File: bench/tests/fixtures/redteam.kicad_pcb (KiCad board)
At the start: 2 copper layers, 40 x 20 mm, 3 parts

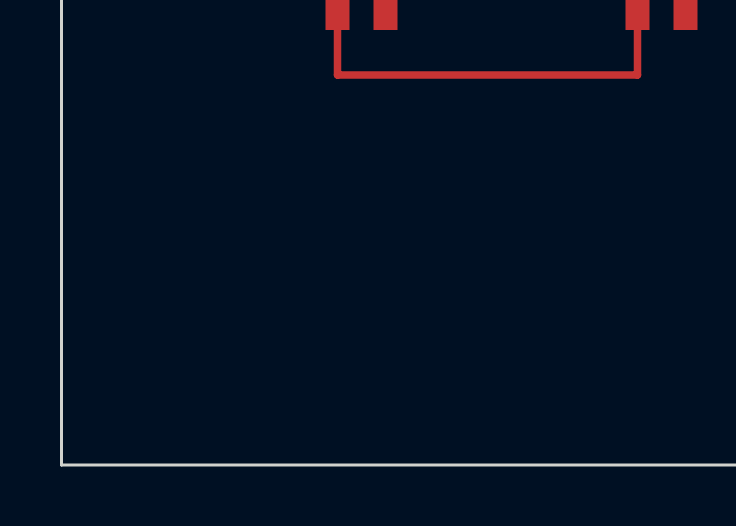
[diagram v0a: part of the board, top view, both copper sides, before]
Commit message: prepare: strip teardrops with the routing; unique footprint uuids (task spec 3)
Found by running the human reference over the 2,491 qualified boards of the
local corpus:

- Teardrops are zones KiCad generates at track ends. strip-routing and
  strip-placement removed the tracks but left the teardrops, so route tasks
  started with stray copper at old track ends, and place tasks kept zones at
  the human pad positions, which leaks the placement being asked for.
  Teardrops are now removed together with the routing.
- Some boards (7 qualified) have footprints sharing a uuid, e.g. all-zero
  placeholders on old-library logos and mounting holes. Everything that
  matches an output to its input goes by footprint uuid, so only one of them
  was moved back and the rest stayed off-board. convert now gives repeated
  footprint uuids unique ones, derived from the original so every task built
  from a board agrees; the task record counts them.
- Placement stats report pads_outside per footprint, and the task record
  keeps the human placement's counts, for judging edge connectors.

Task spec 3; the runner now refuses tasks of any kind prepared under an older
spec. Re-run `prepare --force` and the baselines.

Co-Authored-By: Claude Opus 5.5 <noreply@anthropic.com>
Claude-Session: https://claude.ai/code/session_017mPBGcJJdEJTUCgVtkAC17
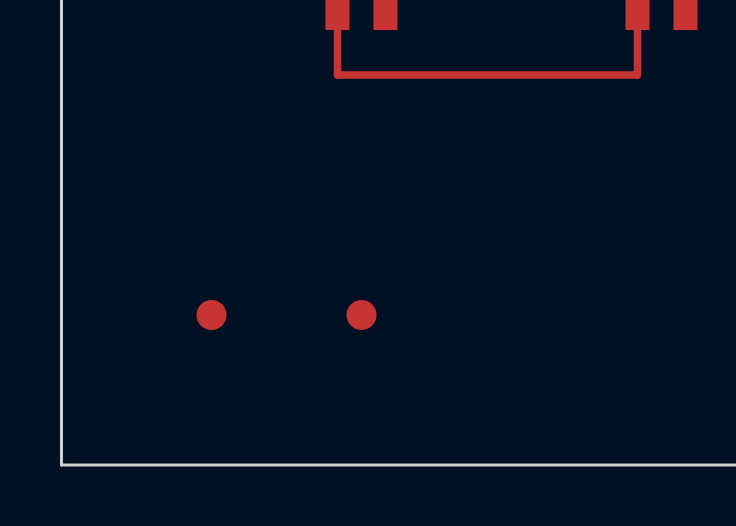
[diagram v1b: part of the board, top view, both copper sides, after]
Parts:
- added TP1: , test:TP, F.Cu at (105.0, 115.0)
- added TP2: , test:TP, F.Cu at (110.0, 115.0)
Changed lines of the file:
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@@
 		(pad "" np_thru_hole circle (at 0 0) (size 3 3) (drill 3) (layers "*.Cu" "*.Mask"))
+	)
+	(footprint "test:TP"
+		(layer "F.Cu")
+		(at 105 115)
+		(property "Reference" "TP1" (at 0 -2 0) (layer "F.Fab") (effects (font (size 1 1) (thickness 0.15))))
+		(fp_rect (start -1 -1) (end 1 1) (stroke (width 0.05) (type solid)) (fill no) (layer "F.CrtYd"))
+		(pad "1" smd circle (at 0 0) (size 1 1) (layers "F.Cu"))
+	)
+	(footprint "test:TP"
+		(layer "F.Cu")
+		(at 110 115)
+		(property "Reference" "TP2" (at 0 -2 0) (layer "F.Fab") (effects (font (size 1 1) (thickness 0.15))))
+		(fp_rect (start -1 -1) (end 1 1) (stroke (width 0.05) (type solid)) (fill no) (layer "F.CrtYd"))
+		(pad "1" smd circle (at 0 0) (size 1 1) (layers "F.Cu"))
 	)
 	(gr_rect (start 100 100) (end 140 120) (stroke (width 0.1) (type solid)) (fill no) (layer "Edge.Cuts"))

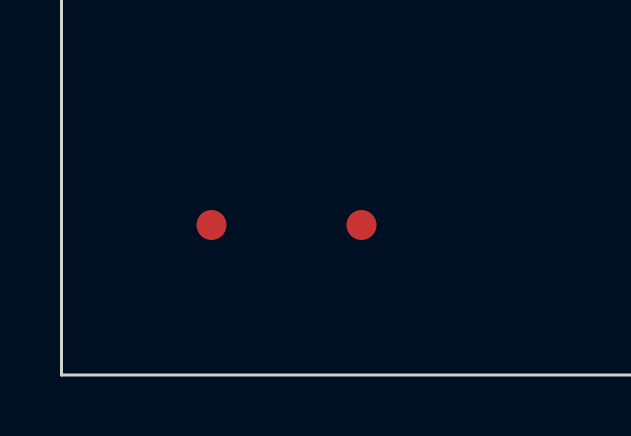
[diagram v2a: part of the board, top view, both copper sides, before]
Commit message: score v5: ignore nets on copper graphics; copy check skips pad-to-pad runs
The score-v4 Freerouting 2.5.0 baseline on the 2,488 qualified corpus boards
had 6 invalid outputs and 2 suspected copies; none was the router's doing:

- Invalid: in all 6, the only "change" was the net of a copper-layer
  graphic (gr_line, gr_arc, gr_circle, gr_poly). KiCad assigns copper
  graphics the net of the tracks that touch them when routing is imported.
  The rebuilt board keeps the input's graphic, so this net never affected a
  score; it is now ignored when comparing. Re-scored, all 6 are valid and 2
  are clean, so the v4 baseline undercounts Freerouting by 2 boards.
- Suspect: a breadboard (504 of 716 tracks matched the human layout, every
  one a straight pad-to-pad strip, which any router draws) and a board most
  likely autorouted with Freerouting by its designer. Straight segments
  between two pad centres no longer count towards `copy`; the breadboard
  drops to 0.0 and the other to 0.58. The copy check stays report-only: a
  board its designer autorouted will match whatever router reproduces it.

Red-team case: giving a copper graphic a net leaves the result valid and
clean. Attempts record score_version=5; re-score the baselines.

Co-Authored-By: Claude Opus 5.5 <noreply@anthropic.com>
Claude-Session: https://claude.ai/code/session_017mPBGcJJdEJTUCgVtkAC17
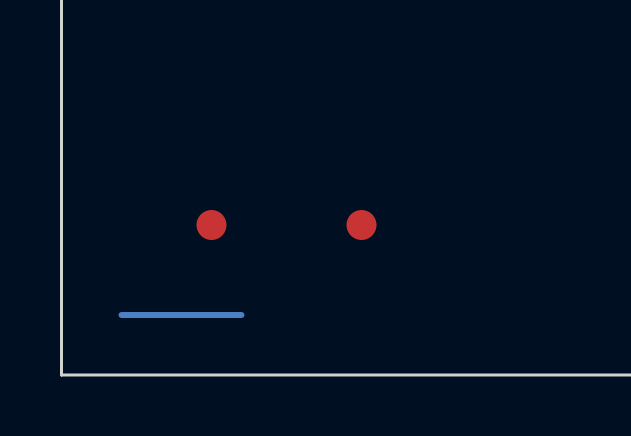
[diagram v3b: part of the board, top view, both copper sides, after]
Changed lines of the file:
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@@
 		(pad "1" smd circle (at 0 0) (size 1 1) (layers "F.Cu"))
 	)
+	(gr_line (start 102 118) (end 106 118) (stroke (width 0.2) (type solid)) (layer "B.Cu"))
 	(gr_rect (start 100 100) (end 140 120) (stroke (width 0.1) (type solid)) (fill no) (layer "Edge.Cuts"))
 	(zone

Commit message: prepare: keep footprints carrying Edge.Cuts in place in place tasks (task spec 5)
strip-placement staged every unlocked footprint off-board, including ones
whose Edge.Cuts graphics are part of the board outline: switch cut-outs,
slots, card edges. Reported by the placement session, which audited the
112-board manifest set: 11 boards had such a footprint unlocked. On those,
the place-task outline lost its holes (e.g. 16 -> 0 and 28 -> 0 cut-outs),
4 outlines were left open, and the staged cut-outs became extra closed
outline polygons in the staging area, so a pads-inside-outline check
accepted pads placed on area that is not board.

Such footprints are now anchored like locked ones: they stay where the
designer put them, and the scorer requires them unmoved (reported as
locked_moved). Placement stats report `anchored`. Task spec 5; re-prepare
place tasks and re-run place baselines. Red-team fixture gains an unlocked
slot footprint and a cheat that moves it.

Co-Authored-By: Claude Opus 5.5 <noreply@anthropic.com>
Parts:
- added SL1: , test:SLOT, F.Cu at (125.0, 114.0)
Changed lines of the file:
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@@
 	)
 	(gr_line (start 102 118) (end 106 118) (stroke (width 0.2) (type solid)) (layer "B.Cu"))
+	(footprint "test:SLOT"
+		(layer "F.Cu")
+		(at 125 114)
+		(property "Reference" "SL1" (at 0 -2 0) (layer "F.Fab") (effects (font (size 1 1) (thickness 0.15))))
+		(fp_rect (start -2 -0.5) (end 2 0.5) (stroke (width 0.1) (type solid)) (fill no) (layer "Edge.Cuts"))
+	)
 	(gr_rect (start 100 100) (end 140 120) (stroke (width 0.1) (type solid)) (fill no) (layer "Edge.Cuts"))
 	(zone

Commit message: place-fixed and joint-fixed tasks: the mechanical interface stays at the human pose
A place task frees every unlocked footprint, connectors and mounting holes included, so a
placer can beat the human on metrics with a board that no longer fits its enclosure or
cables. place-fixed keeps the board's mechanical interface where the designer put it and
places everything else; joint-fixed places and routes from the same input.

- kicad_scripts/mech_rules.py: auditable classifier (connector / mounting / user), first
  matching rule wins: exclusions (test points, jumpers, net ties, heatsinks, no pads), KiCad
  library, all-NPTH, THT LED name, passive/IC conflicts, footprint-name patterns, symbol
  names as values, reference prefixes checked against the footprint. Every rule is
  documented in the module and the README.
- pcbnew ops classify-mech (per footprint: uuid, ref, fpid, value, class, evidence) and
  lock-footprints.
- prepare builds place-fixed/{reference,human-placement,input}: the fixed parts are locked,
  so the existing anchored/locked logic of strip_placement and transplant_placement
  (locked_moved) applies unchanged. The record keeps input_stats, input_drc, movable,
  fixed_mech with class and evidence, and the overrides applied
  (--fixed-overrides FILE: {id: {fix: [refs], free: [refs]}}).
- TASK_SPEC 7; the new kinds need spec 7, the minimums of route/place/joint are unchanged.
  The place-fixed round trip is recorded but does not decide qualification; runs skip only
  the fixed kinds of a board that fails it.
- score_place_task/score_joint_task take the task kind (default place), runner/report/cli
  accept the new kinds, --min-movable applies to them, human-freerouting runs joint-fixed.

Scoring and integrity code: score.py and prepare.py are only parametrized by kind and
pcbnew_ops.py only gains two ops; place, route and joint inputs, scores and qualification
are unchanged (all existing tests pass). The red-team fixture gains a connector, a button
and an 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
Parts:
- added H2: MountingHole, MountingHole:MountingHole_2.2mm_M2, F.Cu at (135.0, 105.0)
- added J1: Conn_01x02, Connector_PinHeader_2.54mm:PinHeader_1x02_P2.54mm_Vertical, F.Cu at (130.0, 103.0)
- added SW1: SW_Push, Button_Switch_SMD:SW_Push_Test, F.Cu at (103.5, 108.0)
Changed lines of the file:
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@@
 		(pad "1" smd circle (at 0 0) (size 1 1) (layers "F.Cu"))
+	)
+	(footprint "Connector_PinHeader_2.54mm:PinHeader_1x02_P2.54mm_Vertical"
+		(layer "F.Cu")
+		(at 130 103)
+		(property "Reference" "J1" (at 0 -2.5 0) (layer "F.Fab") (effects (font (size 1 1) (thickness 0.15))))
+		(property "Value" "Conn_01x02" (at 0 2.5 0) (layer "F.Fab") (effects (font (size 1 1) (thickness 0.15))))
+		(fp_rect (start -2.5 -1.5) (end 2.5 1.5) (stroke (width 0.05) (type solid)) (fill no) (layer "F.CrtYd"))
+		(pad "1" smd rect (at -1.27 0) (size 1 1.5) (layers "F.Cu"))
+		(pad "2" smd rect (at 1.27 0) (size 1 1.5) (layers "F.Cu"))
+	)
+	(footprint "Button_Switch_SMD:SW_Push_Test"
+		(layer "F.Cu")
+		(at 103.5 108)
+		(property "Reference" "SW1" (at 0 -2.5 0) (layer "F.Fab") (effects (font (size 1 1) (thickness 0.15))))
+		(property "Value" "SW_Push" (at 0 2.5 0) (layer "F.Fab") (effects (font (size 1 1) (thickness 0.15))))
+		(fp_rect (start -2 -1.5) (end 2 1.5) (stroke (width 0.05) (type solid)) (fill no) (layer "F.CrtYd"))
+		(pad "1" smd rect (at -1.5 0) (size 1 1) (layers "F.Cu"))
+		(pad "2" smd rect (at 1.5 0) (size 1 1) (layers "F.Cu"))
+	)
+	(footprint "MountingHole:MountingHole_2.2mm_M2"
+		(layer "F.Cu")
+		(at 135 105)
+		(property "Reference" "H2" (at 0 -3 0) (layer "F.Fab") (effects (font (size 1 1) (thickness 0.15))))
+		(property "Value" "MountingHole" (at 0 3 0) (layer "F.Fab") (effects (font (size 1 1) (thickness 0.15))))
+		(fp_circle (center 0 0) (end 2 0) (stroke (width 0.05) (type solid)) (fill no) (layer "F.CrtYd"))
+		(pad "" np_thru_hole circle (at 0 0) (size 2.2 2.2) (drill 2.2) (layers "*.Cu" "*.Mask"))
 	)
 	(gr_line (start 102 118) (end 106 118) (stroke (width 0.2) (type solid)) (layer "B.Cu"))
